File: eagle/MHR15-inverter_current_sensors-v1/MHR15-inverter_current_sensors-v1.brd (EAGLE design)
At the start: 142 x 22.5 mm, 7 parts

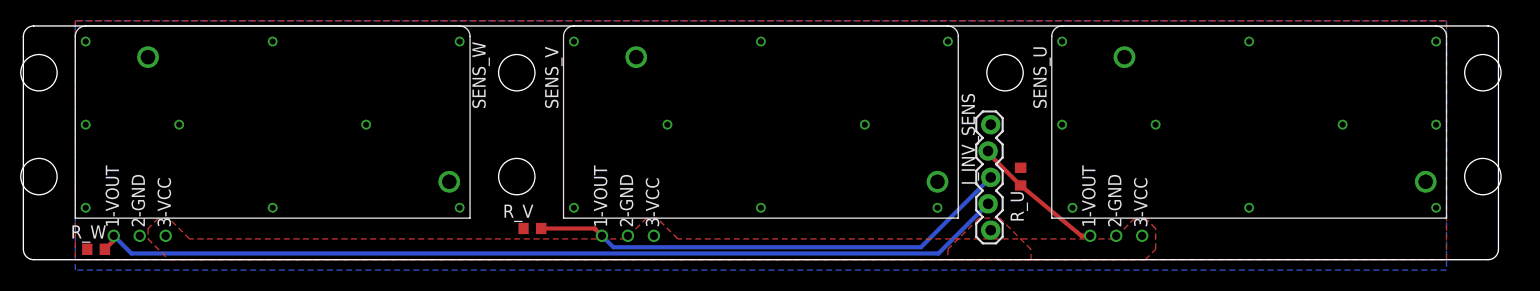
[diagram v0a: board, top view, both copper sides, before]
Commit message: updated current sensor board and GLV_PWR simulation
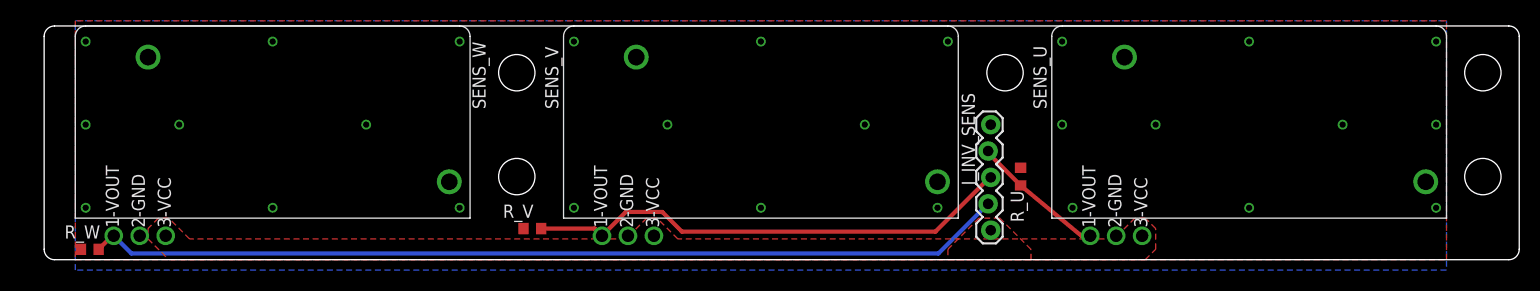
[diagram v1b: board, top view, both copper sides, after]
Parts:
- moved R_W 0.60 mm to (6.40, 1.00)
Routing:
- net SENS_V: track 46.8 -> 47.5 mm
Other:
- board text added: "MHR-15 Inverter Current Sensor PCB v1 (c) 2015 Ben Wang 12/31/14"
- board text removed: "MHR-15 Inverter Current Sensor PCB v1 (c) 2014 Ben Wang 12/30/14"
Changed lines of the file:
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@@
 <board>
 <plain>
-<wire x1="0" y1="21.5" x2="0" y2="1" width="0" layer="20"/>
-<wire x1="0" y1="1" x2="1" y2="0" width="0" layer="20" curve="90"/>
-<wire x1="1" y1="0" x2="141" y2="0" width="0" layer="20"/>
-<wire x1="141" y1="0" x2="142" y2="1" width="0" layer="20" curve="90"/>
-<wire x1="142" y1="1" x2="142" y2="21.5" width="0" layer="20"/>
-<wire x1="142" y1="21.5" x2="141" y2="22.5" width="0" layer="20" curve="90"/>
-<wire x1="141" y1="22.5" x2="1" y2="22.5" width="0" layer="20"/>
-<wire x1="1" y1="22.5" x2="0" y2="21.5" width="0" layer="20" curve="90"/>
+<wire x1="143" y1="22.5" x2="3" y2="22.5" width="0" layer="20"/>
+<wire x1="3" y1="22.5" x2="2" y2="21.5" width="0" layer="20" curve="90"/>
+<wire x1="2" y1="21.5" x2="2" y2="1" width="0" layer="20"/>
+<wire x1="2" y1="1" x2="3" y2="0" width="0" layer="20" curve="90"/>
+<wire x1="3" y1="0" x2="143" y2="0" width="0" layer="20"/>
+<wire x1="143" y1="0" x2="144" y2="1" width="0" layer="20" curve="90"/>
+<wire x1="144" y1="1" x2="144" y2="21.5" width="0" layer="20"/>
+<wire x1="144" y1="21.5" x2="143" y2="22.5" width="0" layer="20" curve="90"/>
 <text x="78" y="6" size="1.778" layer="26" rot="MR0">MHR-15 Inverter Current Sensor PCB v1
-(c) 2014 Ben Wang
-12/30/14</text>
+(c) 2015 Ben Wang
+12/31/14</text>
 <polygon width="0.254" layer="26">
 <vertex x="70.820278125" y="19.270978125"/>
@@
 <hole x="47.5" y="18" drill="3.5"/>
 <hole x="47.5" y="8" drill="3.5"/>
-<hole x="1.5" y="18" drill="3.5"/>
-<hole x="1.5" y="8" drill="3.5"/>
 <hole x="94.5" y="18" drill="3.5"/>
 <hole x="140.5" y="18" drill="3.5"/>
 <hole x="140.5" y="8" drill="3.5"/>
-<dimension x1="1" y1="22.5" x2="1" y2="0" x3="-15" y3="11.25" textsize="1.27" layer="47"/>
+<dimension x1="1" y1="22.5" x2="1" y2="0" x3="-1" y3="11.25" textsize="1.27" layer="47"/>
 <dimension x1="47.5" y1="18" x2="94.5" y2="18" x3="71" y3="20" textsize="1.27" layer="28"/>
-<dimension x1="2.5" y1="18" x2="2.5" y2="8" x3="5" y3="13" textsize="1.27" layer="28"/>
-<dimension x1="0" y1="21.5" x2="142" y2="21.5" x3="71" y3="30" textsize="1.27" layer="47" dtype="diameter"/>
-<text x="105" y="31" size="1.27" layer="47" font="vector">Note: All units are in mm</text>
-<dimension x1="1.5" y1="18" x2="47.5" y2="18" x3="24.5" y3="20" textsize="1.27" layer="28"/>
+<dimension x1="2" y1="23.5" x2="144" y2="23.5" x3="73" y3="25.000003125" textsize="1.27" layer="47" dtype="diameter"/>
+<text x="107" y="26" size="1.27" layer="47" font="vector">Note: All units are in mm</text>
 <dimension x1="94.5" y1="18" x2="140.5" y2="18" x3="117.5" y3="20" textsize="1.27" layer="28"/>
 <dimension x1="139.850065625" y1="6.375165625" x2="141.149934375" y2="9.624834375" x3="138" y3="9.000003125" textsize="1.27" layer="28" dtype="diameter"/>
 <text x="135" y="16" size="1.27" layer="28" font="vector" rot="MR0">Note: All units are in mm.
 Board size: 142x22.5mm</text>
+<dimension x1="140.5" y1="18" x2="140.5" y2="8" x3="143" y3="13" textsize="1.778" layer="28"/>
 </plain>
 <attributes>
@@
 <attribute name="NAME" x="98.5" y="14.5" size="1.27" layer="25" rot="R90"/>
 </element>
-<element name="R_W" library="rcl" package="R0603" value="10k" x="7" y="1" smashed="yes">
-<attribute name="NAME" x="4.565" y="2.035" size="1.27" layer="25"/>
-<attribute name="VALUE" x="8.765" y="0.395" size="1.27" layer="27"/>
+<element name="R_W" library="rcl" package="R0603" value="10k" x="6.4" y="1" smashed="yes">
+<attribute name="NAME" x="3.965" y="2.035" size="1.27" layer="25"/>
+<attribute name="VALUE" x="8.165" y="0.395" size="1.27" layer="27"/>
 </element>
 <element name="R_V" library="rcl" package="R0603" value="10k" x="49" y="3" smashed="yes">
@@
 <wire x1="92.873" y1="5.38" x2="88.093" y2="0.6" width="0.4064" layer="16"/>
 <wire x1="88.093" y1="0.6" x2="10.4" y2="0.6" width="0.4064" layer="16"/>
-<wire x1="8.7" y1="2.3" x2="8.7" y2="1.85" width="0.4064" layer="1"/>
-<wire x1="8.7" y1="1.85" x2="7.85" y2="1" width="0.4064" layer="1"/>
+<wire x1="8.7" y1="2.3" x2="8.55" y2="2.3" width="0.4064" layer="1"/>
+<wire x1="8.55" y1="2.3" x2="7.25" y2="1" width="0.4064" layer="1"/>
 </signal>
 <signal name="SENS_U">
@@
 <wire x1="49.85" y1="3" x2="55" y2="3" width="0.4064" layer="1"/>
 <wire x1="55" y1="3" x2="55.7" y2="2.3" width="0.4064" layer="1"/>
-<wire x1="93.127" y1="7.92" x2="86.407" y2="1.2" width="0.4064" layer="16"/>
-<wire x1="86.407" y1="1.2" x2="56.8" y2="1.2" width="0.4064" layer="16"/>
-<wire x1="56.8" y1="1.2" x2="55.7" y2="2.3" width="0.4064" layer="16"/>
+<wire x1="93.127" y1="7.92" x2="93.02" y2="7.92" width="0.4064" layer="1"/>
+<wire x1="93.02" y1="7.92" x2="87.8" y2="2.7" width="0.4064" layer="1"/>
+<wire x1="87.8" y1="2.7" x2="63.4" y2="2.7" width="0.4064" layer="1"/>
+<wire x1="63.4" y1="2.7" x2="61.5" y2="4.6" width="0.4064" layer="1"/>
+<wire x1="61.5" y1="4.6" x2="58" y2="4.6" width="0.4064" layer="1"/>
+<wire x1="58" y1="4.6" x2="55.7" y2="2.3" width="0.4064" layer="1"/>
 </signal>
 </signals>

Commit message: updated board, but this version violates clearance
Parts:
- moved SENS_U 94.0 mm to (26.5, 7.50)
- moved SENS_W 94.0 mm to (120.5, 7.50)
- moved R_U 89.9 mm to (6.40, 1.00), turned to 0 degrees
- moved R_W 89.9 mm to (96.0, 8.00), turned to 270 degrees
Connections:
- net SENS_U: now also J_INV_SENS.4; no longer J_INV_SENS.2
- net SENS_W: now also J_INV_SENS.2; no longer J_INV_SENS.4
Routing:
- net SENS_W: track 88.8 -> 13.1 mm
- net SENS_U: track 13.1 -> 86.4 mm
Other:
- board text added: "MHR-15 Inverter Current Sensor PCB v1 (c) 2015 Ben Wang 1/16/15"
- board text removed: "MHR-15 Inverter Current Sensor PCB v1 (c) 2015 Ben Wang 12/31/14"
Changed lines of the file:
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@@
 <text x="78" y="6" size="1.778" layer="26" rot="MR0">MHR-15 Inverter Current Sensor PCB v1
 (c) 2015 Ben Wang
-12/31/14</text>
+1/16/15</text>
 <polygon width="0.254" layer="26">
 <vertex x="70.820278125" y="19.270978125"/>
@@
 </autorouter>
 <elements>
-<element name="SENS_W" library="MHR15-TS" package="L01Z400S05" value="L01Z400S05" x="26.5" y="7.5" smashed="yes">
+<element name="SENS_U" library="MHR15-TS" package="L01Z400S05" value="L01Z400S05" x="26.5" y="7.5" smashed="yes">
 <attribute name="MFC_PN" value="L01Z400S05" x="56.98" y="-42.03" size="1.778" layer="27" display="off"/>
 <attribute name="MANUFACTURER" value="Tamura" x="56.98" y="-42.03" size="1.778" layer="27" display="off"/>
@@
 <attribute name="NAME" x="51.5" y="14.5" size="1.27" layer="25" rot="R90"/>
 </element>
-<element name="SENS_U" library="MHR15-TS" package="L01Z400S05" value="L01Z400S05" x="120.5" y="7.5" smashed="yes">
+<element name="SENS_W" library="MHR15-TS" package="L01Z400S05" value="L01Z400S05" x="120.5" y="7.5" smashed="yes">
 <attribute name="MFC_PN" value="L01Z400S05" x="150.98" y="1.15" size="1.778" layer="27" display="off"/>
 <attribute name="MANUFACTURER" value="Tamura" x="150.98" y="1.15" size="1.778" layer="27" display="off"/>
@@
 <attribute name="NAME" x="98.5" y="14.5" size="1.27" layer="25" rot="R90"/>
 </element>
-<element name="R_W" library="rcl" package="R0603" value="10k" x="6.4" y="1" smashed="yes">
+<element name="R_U" library="rcl" package="R0603" value="10k" x="6.4" y="1" smashed="yes">
 <attribute name="NAME" x="3.965" y="2.035" size="1.27" layer="25"/>
 <attribute name="VALUE" x="8.165" y="0.395" size="1.27" layer="27"/>
@@
 <attribute name="VALUE" x="48.365" y="1.095" size="1.27" layer="27"/>
 </element>
-<element name="R_U" library="rcl" package="R0603" value="10k" x="96" y="8" smashed="yes" rot="R270">
+<element name="R_W" library="rcl" package="R0603" value="10k" x="96" y="8" smashed="yes" rot="R270">
 <attribute name="NAME" x="95.035" y="6.635" size="1.27" layer="25" rot="R270"/>
 <attribute name="VALUE" x="94.995" y="13.035" size="1.27" layer="27" rot="R270"/>
@@
 <contactref element="SENS_W" pad="VOUT"/>
 <contactref element="R_W" pad="2"/>
-<contactref element="J_INV_SENS" pad="4"/>
-<wire x1="8.7" y1="2.3" x2="10.4" y2="0.6" width="0.4064" layer="16"/>
-<wire x1="92.873" y1="5.38" x2="88.093" y2="0.6" width="0.4064" layer="16"/>
-<wire x1="88.093" y1="0.6" x2="10.4" y2="0.6" width="0.4064" layer="16"/>
-<wire x1="8.7" y1="2.3" x2="8.55" y2="2.3" width="0.4064" layer="1"/>
-<wire x1="8.55" y1="2.3" x2="7.25" y2="1" width="0.4064" layer="1"/>
+<wire x1="96" y1="7.15" x2="101.85" y2="2.3" width="0.4064" layer="1"/>
+<wire x1="101.85" y1="2.3" x2="102.7" y2="2.3" width="0.4064" layer="1"/>
+<contactref element="J_INV_SENS" pad="2"/>
+<wire x1="92.873" y1="10.46" x2="92.873" y2="10.277" width="0.4064" layer="1"/>
+<wire x1="92.873" y1="10.277" x2="96" y2="7.15" width="0.4064" layer="1"/>
 </signal>
 <signal name="SENS_U">
 <contactref element="SENS_U" pad="VOUT"/>
 <contactref element="R_U" pad="2"/>
-<contactref element="J_INV_SENS" pad="2"/>
-<wire x1="92.873" y1="10.46" x2="92.873" y2="10.277" width="0.4064" layer="1"/>
-<wire x1="92.873" y1="10.277" x2="96" y2="7.15" width="0.4064" layer="1"/>
-<wire x1="96" y1="7.15" x2="101.85" y2="2.3" width="0.4064" layer="1"/>
-<wire x1="101.85" y1="2.3" x2="102.7" y2="2.3" width="0.4064" layer="1"/>
+<wire x1="8.7" y1="2.3" x2="8.55" y2="2.3" width="0.4064" layer="1"/>
+<wire x1="8.55" y1="2.3" x2="7.25" y2="1" width="0.4064" layer="1"/>
+<contactref element="J_INV_SENS" pad="4"/>
+<wire x1="92.873" y1="5.38" x2="88.093" y2="0.6" width="0.4064" layer="16"/>
+<wire x1="88.093" y1="0.6" x2="10.4" y2="0.6" width="0.4064" layer="16"/>
+<wire x1="8.7" y1="2.3" x2="10.4" y2="0.6" width="0" layer="19" extent="16-16"/>
 </signal>
 <signal name="5VDC">
+<contactref element="SENS_U" pad="VCC"/>
 <contactref element="SENS_W" pad="VCC"/>
-<contactref element="SENS_U" pad="VCC"/>
 <contactref element="SENS_V" pad="VCC"/>
 <contactref element="J_INV_SENS" pad="5"/>
@@
 </signal>
 <signal name="GND">
+<contactref element="SENS_U" pad="GND"/>
+<contactref element="R_U" pad="1"/>
+<contactref element="SENS_V" pad="GND"/>
+<contactref element="R_V" pad="1"/>
 <contactref element="SENS_W" pad="GND"/>
 <contactref element="R_W" pad="1"/>
-<contactref element="SENS_V" pad="GND"/>
-<contactref element="R_V" pad="1"/>
-<contactref element="SENS_U" pad="GND"/>
-<contactref element="R_U" pad="1"/>
 <polygon width="0.4064" layer="16">
-<vertex x="5" y="23"/>
-<vertex x="137" y="23"/>
+<vertex x="5" y="-1"/>
+<vertex x="5" y="14" curve="-90"/>
+<vertex x="6" y="15"/>
+<vertex x="136" y="15" curve="-90"/>
+<vertex x="137" y="14"/>
 <vertex x="137" y="-1"/>
-<vertex x="5" y="-1"/>
 </polygon>
 <polygon width="0.4064" layer="1" rank="3">
-<vertex x="137" y="23"/>
-<vertex x="5" y="23"/>
+<vertex x="137" y="0"/>
+<vertex x="137" y="14" curve="90"/>
+<vertex x="136" y="15"/>
+<vertex x="6" y="15" curve="90"/>
+<vertex x="5" y="14"/>
 <vertex x="5" y="0"/>
-<vertex x="137" y="0"/>
 </polygon>
 <contactref element="J_INV_SENS" pad="1"/>
-<via x="6" y="21" extent="1-16" drill="0.6"/>
 <via x="6" y="13" extent="1-16" drill="0.6"/>
 <via x="6" y="5" extent="1-16" drill="0.6"/>
 <via x="15" y="13" extent="1-16" drill="0.6"/>
-<via x="24" y="21" extent="1-16" drill="0.6"/>
 <via x="33" y="13" extent="1-16" drill="0.6"/>
 <via x="42" y="5" extent="1-16" drill="0.6"/>
-<via x="42" y="21" extent="1-16" drill="0.6"/>
 <via x="24" y="5" extent="1-16" drill="0.6"/>
-<via x="53" y="21" extent="1-16" drill="0.6"/>
 <via x="62" y="13" extent="1-16" drill="0.6"/>
 <via x="53" y="5" extent="1-16" drill="0.6"/>
 <via x="71" y="5" extent="1-16" drill="0.6"/>
-<via x="71" y="21" extent="1-16" drill="0.6"/>
 <via x="81" y="13" extent="1-16" drill="0.6"/>
 <via x="88" y="5" extent="1-16" drill="0.6"/>
-<via x="89" y="21" extent="1-16" drill="0.6"/>
-<via x="100" y="21" extent="1-16" drill="0.6"/>
 <via x="100" y="13" extent="1-16" drill="0.6"/>
 <via x="101" y="5" extent="1-16" drill="0.6"/>
 <via x="109" y="13" extent="1-16" drill="0.6"/>
-<via x="118" y="21" extent="1-16" drill="0.6"/>
 <via x="118" y="5" extent="1-16" drill="0.6"/>
 <via x="127" y="13" extent="1-16" drill="0.6"/>
-<via x="136" y="21" extent="1-16" drill="0.6"/>
 <via x="136" y="13" extent="1-16" drill="0.6"/>
 <via x="136" y="5" extent="1-16" drill="0.6"/>

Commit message: finalized v1 of current sensor board
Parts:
- moved SENS_U 94.0 mm to (120.5, 7.50)
- moved SENS_W 94.0 mm to (26.5, 7.50)
- moved R_W 90.9 mm to (5.30, 2.30), turned to 0 degrees
- moved R_U 90.8 mm to (97.0, 7.00), turned to 270 degrees
- moved J_INV_SENS 3.00 mm to (93.0, 16.0)
- moved R_V 3.00 mm to (52.0, 3.00)
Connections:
- net SENS_U: now also J_INV_SENS.2; no longer J_INV_SENS.4
- net SENS_W: now also J_INV_SENS.4; no longer J_INV_SENS.2
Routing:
- net 5VDC: track 0.00 -> 100.5 mm
- net SENS_W: track 13.1 -> 90.3 mm
- net SENS_U: track 86.4 -> 17.2 mm, vias 0 -> 1
- net SENS_V: track 47.5 -> 48.5 mm, vias 0 -> 1
- removed copper zone on layer 1, net 5VDC
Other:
- board size 142 x 22.5 mm -> 142 x 21.5 mm
